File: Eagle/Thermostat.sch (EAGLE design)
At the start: 56 parts, among them J2 USB-MINIB-5PIN, K1 AQY282EHA, K2 AQY282EHA, K3 AQY282EHA, K4 AQY282EHA, K5 AQY282EHA, Q1 MOSFET-PCHANNELSMD

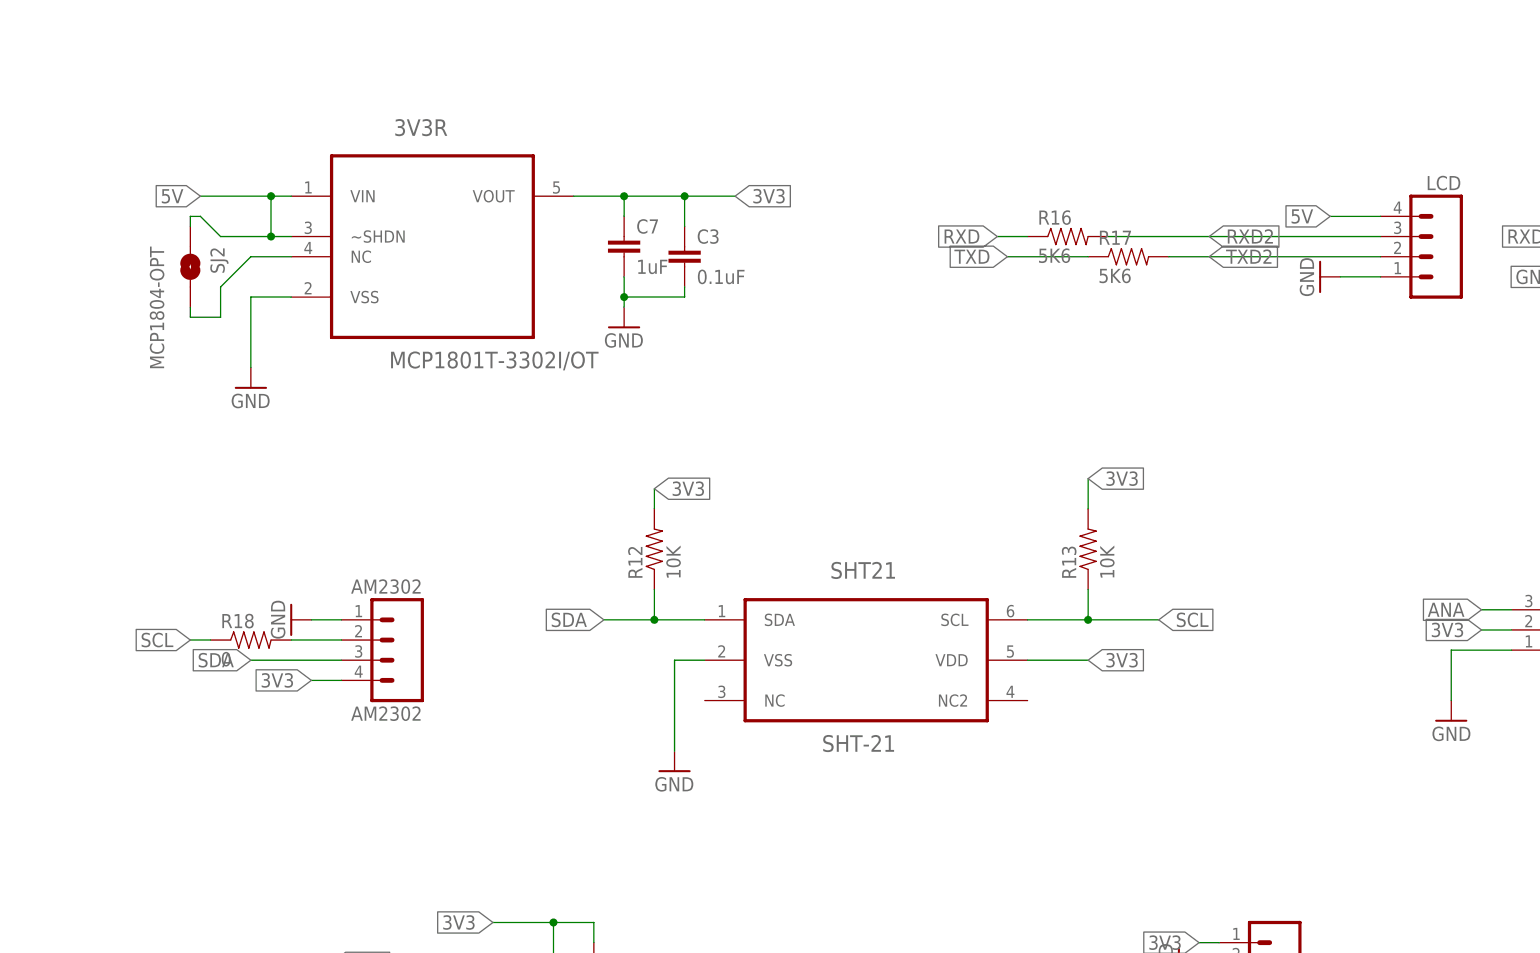
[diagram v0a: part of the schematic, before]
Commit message: Added R19 (optional)
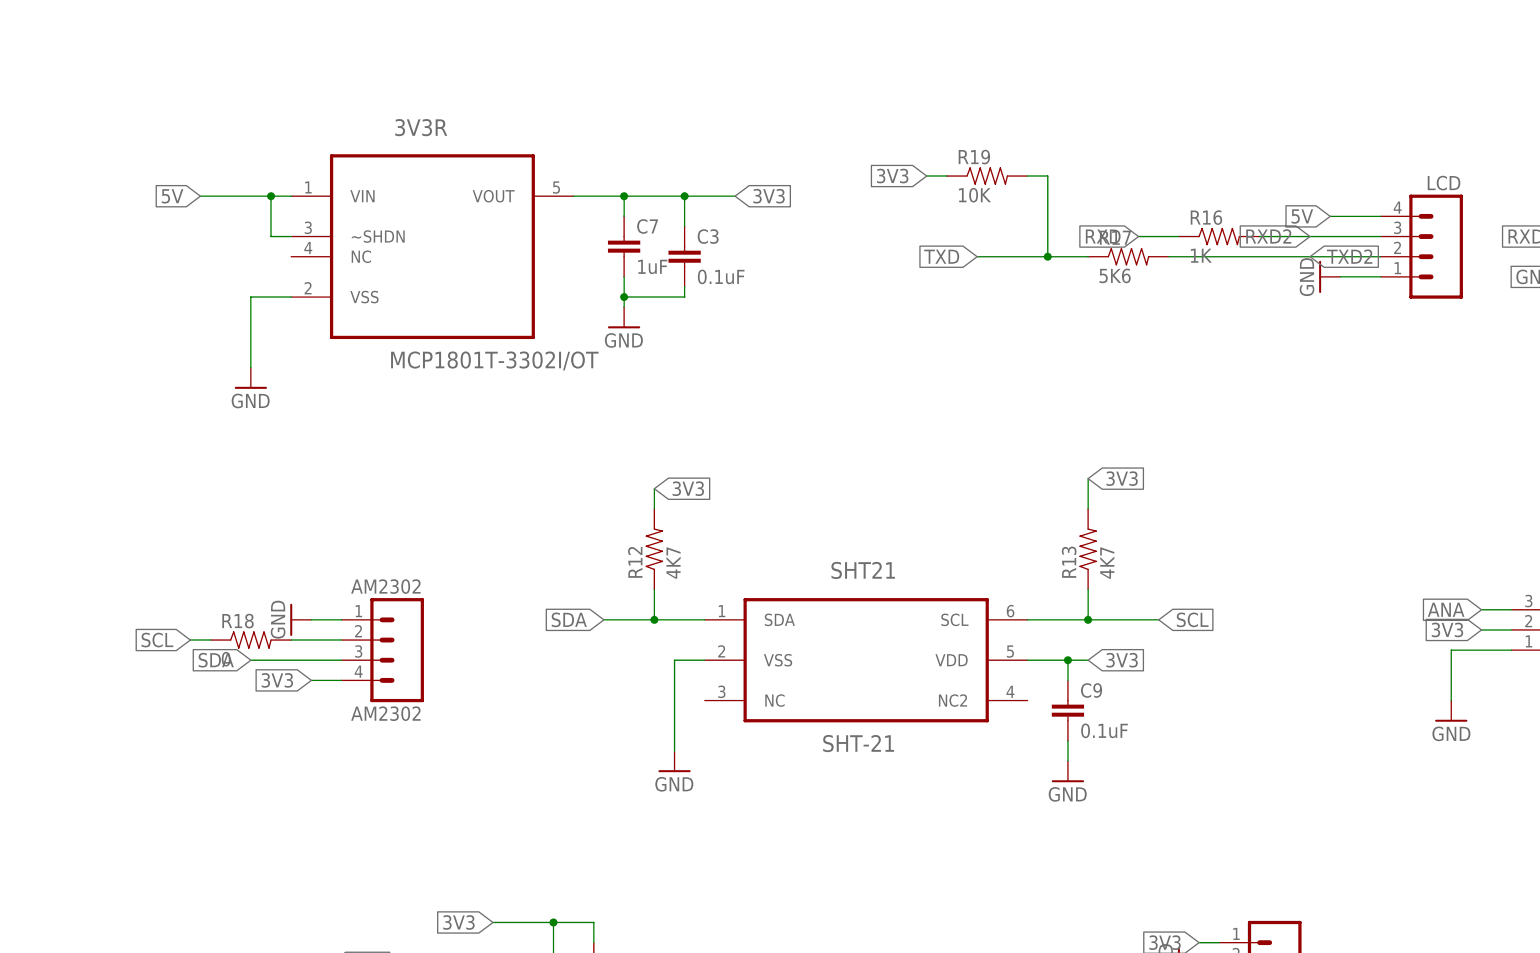
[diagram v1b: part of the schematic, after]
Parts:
- removed SJ2: MCP1804-OPT, SparkFun-Retired:SOLDERJUMPERNO
- added C9: 0.1uF, SparkFun-Capacitors:CAP0805
- added R19: 10K, SparkFun-Resistors:RESISTOR0805-RES
- R12, R13: value 10K -> 4K7
- R16: value 5K6 -> 1K
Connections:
- removed net N$1: 3V3R.NC, SJ2.2
- net 3V3: now also C9.1, R19.1
- net 5V: no longer SJ2.1
- net GND: now also C9.2
- net TXD: now also R19.2
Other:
- moved on the sheet: R16
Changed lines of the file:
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@@
 <part name="Q1" library="SparkFun-DiscreteSemi" deviceset="MOSFET-PCHANNEL" device="SMD"/>
 <part name="GND26" library="supply1" deviceset="GND" device=""/>
-<part name="R12" library="SparkFun-Resistors" deviceset="RESISTOR" device="0805-RES" value="10K"/>
-<part name="R13" library="SparkFun-Resistors" deviceset="RESISTOR" device="0805-RES" value="10K"/>
+<part name="R12" library="SparkFun-Resistors" deviceset="RESISTOR" device="0805-RES" value="4K7"/>
+<part name="R13" library="SparkFun-Resistors" deviceset="RESISTOR" device="0805-RES" value="4K7"/>
 <part name="NEXPRG" library="SparkFun-Connectors" deviceset="M04" device="PTH"/>
 <part name="GND17" library="supply1" deviceset="GND" device=""/>
@@
 <part name="U$5" library="CuriousTech" deviceset="SMD-PAD1" device=""/>
 <part name="GND27" library="supply1" deviceset="GND" device=""/>
-<part name="R16" library="SparkFun-Resistors" deviceset="RESISTOR" device="0805-RES" value="5K6"/>
+<part name="R16" library="SparkFun-Resistors" deviceset="RESISTOR" device="0805-RES" value="1K"/>
 <part name="J1" library="SparkFun-Connectors" deviceset="M03" device="PTH"/>
 <part name="J2" library="SparkFun-Connectors" deviceset="USB-MINIB" device="-5PIN"/>
 <part name="GND28" library="supply1" deviceset="GND" device=""/>
-<part name="SJ2" library="SparkFun-Retired" deviceset="SOLDERJUMPER" device="NO" value="MCP1804-OPT"/>
 <part name="5VSWPP" library="CuriousTech" deviceset="MIC4680" device=""/>
 <part name="C8" library="SparkFun-Capacitors" deviceset="CAP" device="0805" value="1uF"/>
@@
 <part name="5V" library="SparkFun-Connectors" deviceset="M01" device="PTH"/>
 <part name="SHT21" library="CuriousTech" deviceset="SHT-21" device=""/>
+<part name="C9" library="SparkFun-Capacitors" deviceset="CAP" device="0805" value="0.1uF"/>
+<part name="GND29" library="supply1" deviceset="GND" device=""/>
+<part name="R19" library="SparkFun-Resistors" deviceset="RESISTOR" device="0805-RES" value="10K"/>
 </parts>
 <sheets>
@@
 <instance part="U$5" gate="G$1" x="406.4" y="142.24"/>
 <instance part="GND27" gate="1" x="397.51" y="132.08" rot="MR0"/>
-<instance part="R16" gate="G$1" x="270.51" y="158.75"/>
+<instance part="R16" gate="G$1" x="289.56" y="158.75"/>
 <instance part="J1" gate="J$1" x="334.01" y="109.22" rot="MR0"/>
 <instance part="J2" gate="G$1" x="356.87" y="104.14"/>
 <instance part="GND28" gate="1" x="361.95" y="88.9" rot="MR0"/>
-<instance part="SJ2" gate="1" x="160.02" y="154.94" rot="R270"/>
 <instance part="5VSWPP" gate="G$1" x="80.01" y="168.91" rot="R90"/>
 <instance part="C8" gate="G$1" x="124.46" y="140.97"/>
@@
 <instance part="5V" gate="G$1" x="124.46" y="165.1" rot="R270"/>
 <instance part="SHT21" gate="G$1" x="245.11" y="105.41"/>
+<instance part="C9" gate="G$1" x="270.51" y="97.79"/>
+<instance part="GND29" gate="1" x="270.51" y="90.17"/>
+<instance part="R19" gate="G$1" x="260.35" y="166.37"/>
 </instances>
 <busses>
@@
 <junction x="359.41" y="95.25"/>
 </segment>
+<segment>
+<pinref part="GND29" gate="1" pin="GND"/>
+<pinref part="C9" gate="G$1" pin="2"/>
+<wire x1="270.51" y1="92.71" x2="270.51" y2="95.25" width="0.1524" layer="91"/>
+</segment>
 </net>
 <net name="N$24" class="0">
@@
 </segment>
 <segment>
-<wire x1="265.43" y1="105.41" x2="273.05" y2="105.41" width="0.1524" layer="91"/>
+<wire x1="265.43" y1="105.41" x2="270.51" y2="105.41" width="0.1524" layer="91"/>
 <label x="273.05" y="105.41" size="1.778" layer="95" xref="yes"/>
 <pinref part="SHT21" gate="G$1" pin="VDD"/>
+<pinref part="C9" gate="G$1" pin="1"/>
+<wire x1="270.51" y1="105.41" x2="273.05" y2="105.41" width="0.1524" layer="91"/>
+<wire x1="270.51" y1="102.87" x2="270.51" y2="105.41" width="0.1524" layer="91"/>
+<junction x="270.51" y="105.41"/>
 </segment>
 <segment>
@@
 <label x="322.58" y="109.22" size="1.778" layer="95" rot="R180" xref="yes"/>
 </segment>
+<segment>
+<pinref part="R19" gate="G$1" pin="1"/>
+<wire x1="255.27" y1="166.37" x2="252.73" y2="166.37" width="0.1524" layer="91"/>
+<label x="252.73" y="166.37" size="1.778" layer="95" rot="R180" xref="yes"/>
+</segment>
 </net>
 <net name="TXD" class="0">
@@
 <segment>
 <pinref part="R17" gate="G$1" pin="1"/>
-<wire x1="273.05" y1="156.21" x2="262.89" y2="156.21" width="0.1524" layer="91"/>
-<label x="262.89" y="156.21" size="1.778" layer="95" rot="R180" xref="yes"/>
+<wire x1="273.05" y1="156.21" x2="267.97" y2="156.21" width="0.1524" layer="91"/>
+<label x="259.08" y="156.21" size="1.778" layer="95" rot="R180" xref="yes"/>
+<pinref part="R19" gate="G$1" pin="2"/>
+<wire x1="267.97" y1="156.21" x2="259.08" y2="156.21" width="0.1524" layer="91"/>
+<wire x1="267.97" y1="166.37" x2="265.43" y2="166.37" width="0.1524" layer="91"/>
+<wire x1="267.97" y1="166.37" x2="267.97" y2="156.21" width="0.1524" layer="91"/>
+<junction x="267.97" y="156.21"/>
 </segment>
 </net>
@@
 <segment>
 <pinref part="R16" gate="G$1" pin="1"/>
-<wire x1="265.43" y1="158.75" x2="261.62" y2="158.75" width="0.1524" layer="91"/>
-<label x="261.62" y="158.75" size="1.778" layer="95" rot="R180" xref="yes"/>
+<wire x1="284.48" y1="158.75" x2="279.4" y2="158.75" width="0.1524" layer="91"/>
+<label x="279.4" y="158.75" size="1.778" layer="95" rot="R180" xref="yes"/>
 </segment>
 </net>
@@
 <wire x1="170.18" y1="163.83" x2="172.72" y2="163.83" width="0.1524" layer="91"/>
 <junction x="170.18" y="163.83"/>
-<wire x1="170.18" y1="158.75" x2="163.83" y2="158.75" width="0.1524" layer="91"/>
-<wire x1="163.83" y1="158.75" x2="161.29" y2="161.29" width="0.1524" layer="91"/>
-<junction x="170.18" y="158.75"/>
-<wire x1="161.29" y1="161.29" x2="160.02" y2="161.29" width="0.1524" layer="91"/>
-<pinref part="SJ2" gate="1" pin="1"/>
-<wire x1="160.02" y1="160.02" x2="160.02" y2="161.29" width="0.1524" layer="91"/>
 </segment>
 <segment>
@@
 <pinref part="LCD" gate="G$1" pin="2"/>
 <wire x1="283.21" y1="156.21" x2="309.88" y2="156.21" width="0.1524" layer="91"/>
-<label x="288.29" y="156.21" size="1.778" layer="95" xref="yes"/>
+<label x="300.99" y="156.21" size="1.778" layer="95" xref="yes"/>
 </segment>
 <segment>
@@
 <pinref part="R16" gate="G$1" pin="2"/>
 <pinref part="LCD" gate="G$1" pin="3"/>
-<wire x1="275.59" y1="158.75" x2="309.88" y2="158.75" width="0.1524" layer="91"/>
-<label x="288.29" y="158.75" size="1.778" layer="95" xref="yes"/>
+<label x="300.99" y="158.75" size="1.778" layer="95" rot="R180" xref="yes"/>
+<wire x1="294.64" y1="158.75" x2="309.88" y2="158.75" width="0.1524" layer="91"/>
 </segment>
 <segment>
@@
 </segment>
 </net>
-<net name="N$1" class="0">
-<segment>
-<pinref part="3V3R" gate="A" pin="NC"/>
-<wire x1="172.72" y1="156.21" x2="167.64" y2="156.21" width="0.1524" layer="91"/>
-<wire x1="167.64" y1="156.21" x2="163.83" y2="152.4" width="0.1524" layer="91"/>
-<wire x1="163.83" y1="152.4" x2="163.83" y2="148.59" width="0.1524" layer="91"/>
-<wire x1="163.83" y1="148.59" x2="160.02" y2="148.59" width="0.1524" layer="91"/>
-<pinref part="SJ2" gate="1" pin="2"/>
-<wire x1="160.02" y1="148.59" x2="160.02" y2="149.86" width="0.1524" layer="91"/>
-</segment>
-</net>

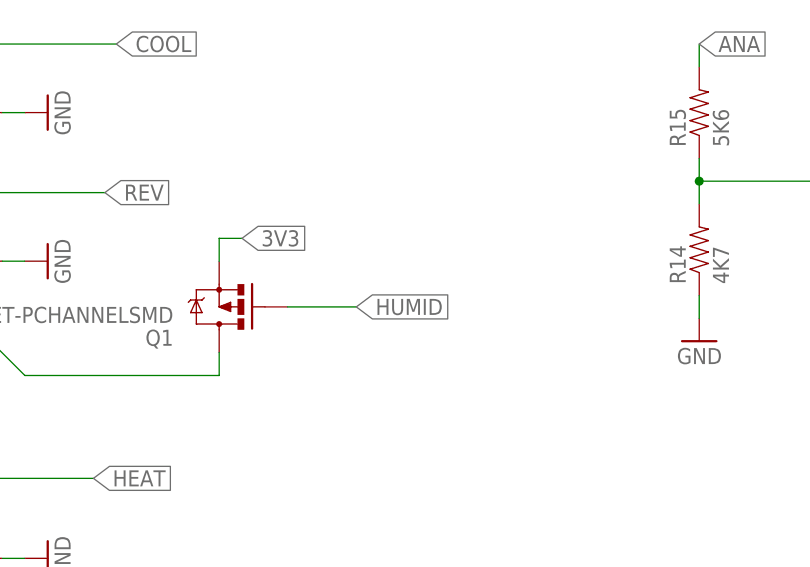
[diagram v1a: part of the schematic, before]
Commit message: Update Thermostat.sch
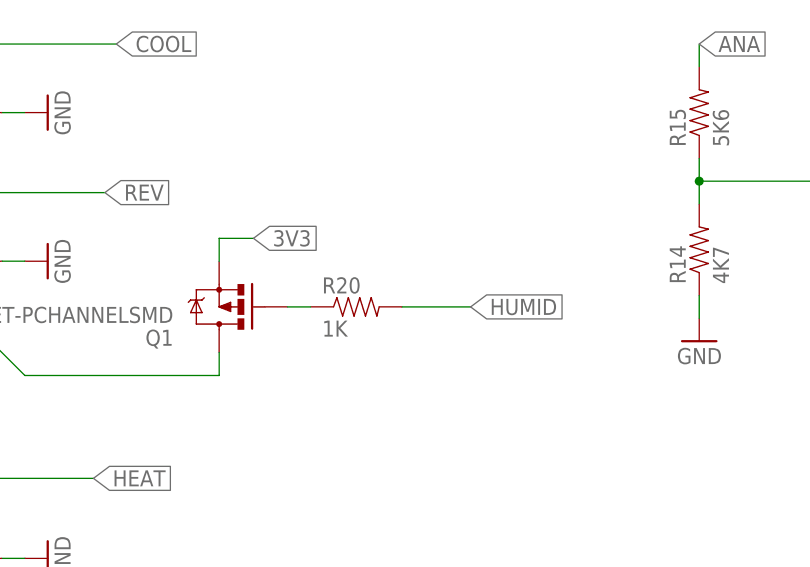
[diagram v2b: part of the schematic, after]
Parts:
- added R20: 1K, SparkFun-Passives:RESISTOR0805-RES
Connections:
- new net N$1: Q1.G, R20.1
- net HUMID: now also R20.2; no longer Q1.G
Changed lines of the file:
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@@
 <part name="GND29" library="supply1" deviceset="GND" device=""/>
 <part name="R19" library="SparkFun-Resistors" deviceset="RESISTOR" device="0805-RES" value="10K"/>
+<part name="R20" library="SparkFun-Passives" deviceset="RESISTOR" device="0805-RES" value="1K"/>
 </parts>
 <sheets>
@@
 <instance part="GND29" gate="1" x="270.51" y="90.17"/>
 <instance part="R19" gate="G$1" x="260.35" y="166.37"/>
+<instance part="R20" gate="G$1" x="139.7" y="38.1"/>
 </instances>
 <busses>
@@
 <pinref part="Q1" gate="G$1" pin="S"/>
 <wire x1="124.46" y1="43.18" x2="124.46" y2="45.72" width="0.1524" layer="91"/>
-<wire x1="124.46" y1="45.72" x2="127" y2="45.72" width="0.1524" layer="91"/>
-<label x="127" y="45.72" size="1.778" layer="95" xref="yes"/>
+<wire x1="124.46" y1="45.72" x2="128.27" y2="45.72" width="0.1524" layer="91"/>
+<label x="128.27" y="45.72" size="1.778" layer="95" xref="yes"/>
 </segment>
 <segment>
@@
 <net name="HUMID" class="0">
 <segment>
-<pinref part="Q1" gate="G$1" pin="G"/>
-<wire x1="132.08" y1="38.1" x2="139.7" y2="38.1" width="0.1524" layer="91"/>
-<label x="139.7" y="38.1" size="1.778" layer="95" xref="yes"/>
-</segment>
-<segment>
 <wire x1="294.64" y1="27.94" x2="294.64" y2="36.83" width="0.1524" layer="91"/>
 <wire x1="269.24" y1="36.83" x2="294.64" y2="36.83" width="0.1524" layer="91"/>
@@
 <pinref part="FLASH" gate="G$1" pin="1"/>
 </segment>
+<segment>
+<pinref part="R20" gate="G$1" pin="2"/>
+<wire x1="144.78" y1="38.1" x2="152.4" y2="38.1" width="0.1524" layer="91"/>
+<label x="152.4" y="38.1" size="1.778" layer="95" xref="yes"/>
+</segment>
 </net>
 <net name="RXD2" class="0">
@@
 </segment>
 </net>
+<net name="N$1" class="0">
+<segment>
+<pinref part="Q1" gate="G$1" pin="G"/>
+<pinref part="R20" gate="G$1" pin="1"/>
+<wire x1="132.08" y1="38.1" x2="134.62" y2="38.1" width="0.1524" layer="91"/>
+</segment>
+</net>
